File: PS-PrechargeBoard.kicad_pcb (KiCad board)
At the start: 2 copper layers, 230 parts, among them IC1 LM74502DDFR, IC2 TCAN3413DR, J1 HV_Main, J10 SWD, J2 HV_Motor, J3 DIAG, J4 CAN_IN, J5 CAN_OUT, J6 DEBUG_NANO, J7 PRECHARGE_CTRL, J8 USB_C_Receptacle_USB2.0_16P, J9 SWD_Header, K1 DE1a-12V, K2 DE1a-12V, Q1 NMOS, Q2 NMOS, Q3 PSMN012-100YS, Q4 PSMN012-100YS, SW1 Reset, SW2 SW_SPDT, U1 TLV9002QDRQ1, U4 TLV9002QDRQ1, U7 MCP1826S, U8 STM32G473CETx, Y1 Crystal

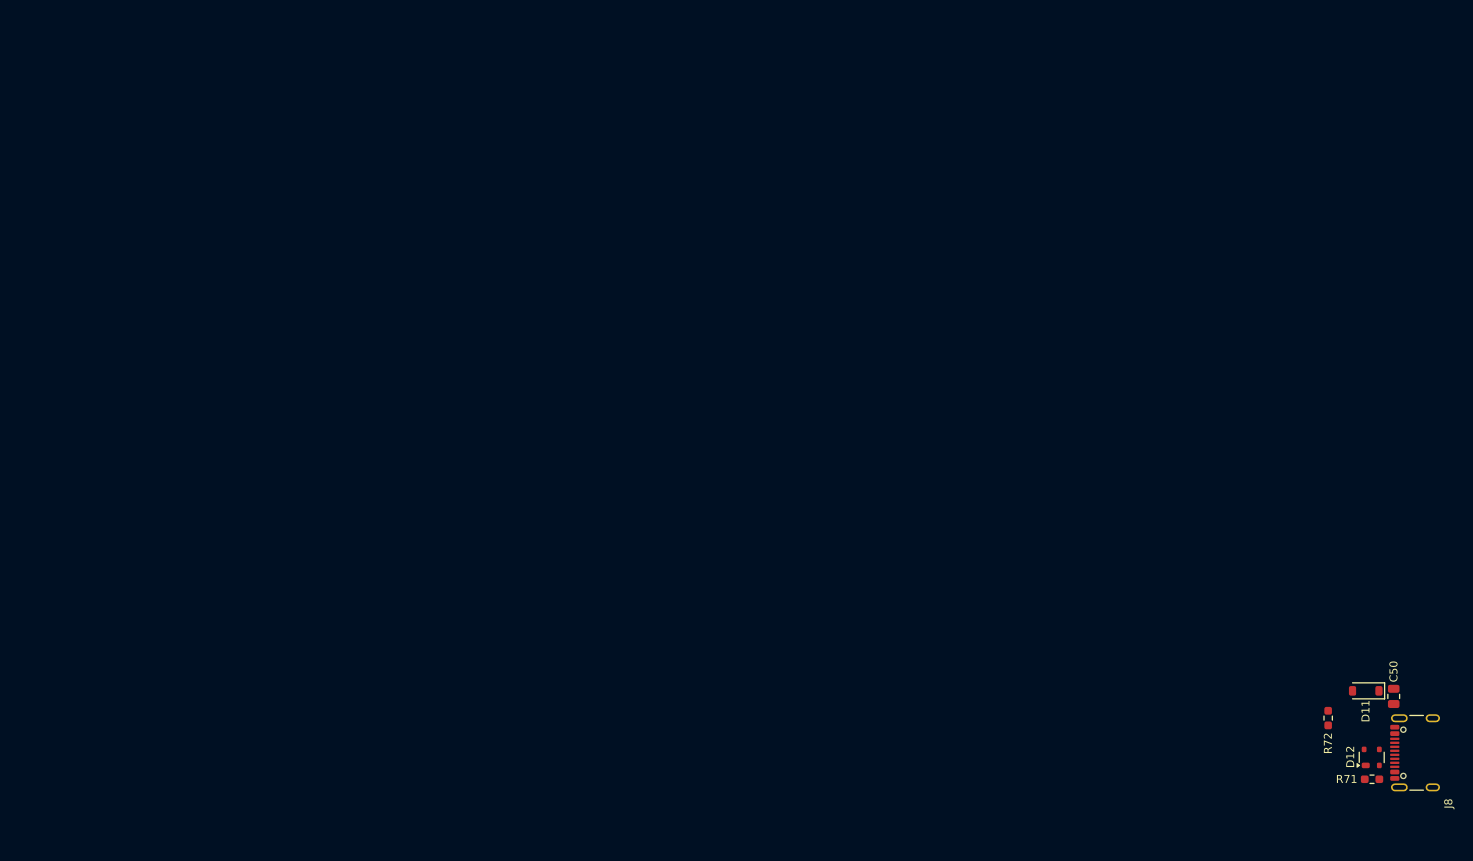
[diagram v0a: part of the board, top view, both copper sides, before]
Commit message: restored usb-c placement
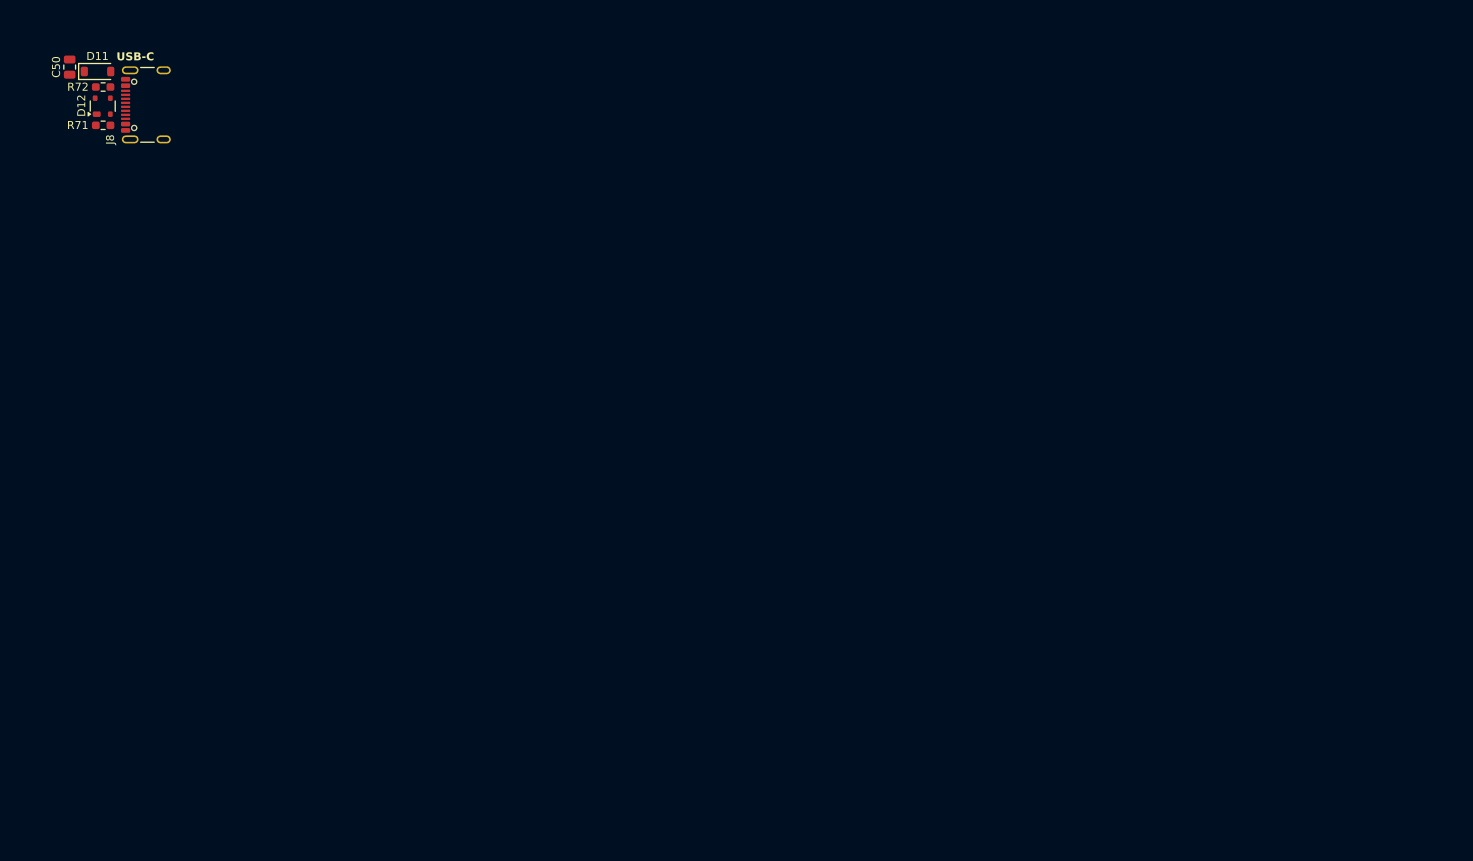
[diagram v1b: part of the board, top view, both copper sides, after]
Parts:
- moved C50 183.2 mm to (175.8, 80.2)
- moved R71 178.4 mm to (179.9, 87.5)
- moved D12 178.3 mm to (179.9, 85.1)
- moved J8 178.1 mm to (186.4, 84.9)
- moved D11 176.4 mm to (179.2, 80.8), turned to 0 degrees
- moved R72 172.3 mm to (179.9, 82.7), turned to 0 degrees
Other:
- board text added: "USB-C"
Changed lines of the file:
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@@
 	(footprint "Capacitor_SMD:C_0805_2012Metric"
 		(layer "F.Cu")
-		(at 341.273 158.886406 -90)
+		(at 175.768 80.222 -90)
 		(descr "Capacitor SMD 0805 (2012 Metric), square (rectangular) end terminal, IPC-7351 nominal, (Body size source: IPC-SM-782 page 76, https://www.pcb-3d.com/wordpress/wp-content/uploads/ipc-sm-782a_amendment_1_and_2.pdf, https://docs.google.com/spreadsheets/d/1BsfQQcO9C6DZCsRaXUlFlo91Tg2WpOkGARC1WS5S8t0/edit?usp=sharing)")
 		(tags "capacitor")
 		(property "Reference" "C50"
-			(at -3.109 0 90)
+			(at -0.0088 1.6764 90)
 			(layer "F.SilkS")
 			(effects
@@
 	(footprint "Resistor_SMD:R_0603_1608Metric_Pad0.98x0.95mm_HandSolder"
 		(layer "F.Cu")
-		(at 338.5615 169.241406)
+		(at 179.948 87.499667)
 		(descr "Resistor SMD 0603 (1608 Metric), square (rectangular) end terminal, IPC-7351 nominal with elongated pad for handsoldering. (Body size source: IPC-SM-782 page 72, https://www.pcb-3d.com/wordpress/wp-content/uploads/ipc-sm-782a_amendment_1_and_2.pdf)")
 		(tags "resistor handsolder")
@@
 	(footprint "Package_TO_SOT_SMD:SOT-143"
 		(layer "F.Cu")
-		(at 338.522 166.513406 90)
+		(at 179.898 85.106 90)
 		(descr "SOT-143 https://www.nxp.com/docs/en/package-information/SOT143B.pdf")
 		(tags "SOT-143")
@@
 	(footprint "Resistor_SMD:R_0603_1608Metric_Pad0.98x0.95mm_HandSolder"
 		(layer "F.Cu")
-		(at 333.077 161.597906 90)
+		(at 179.948 82.712334)
 		(descr "Resistor SMD 0603 (1608 Metric), square (rectangular) end terminal, IPC-7351 nominal with elongated pad for handsoldering. (Body size source: IPC-SM-782 page 72, https://www.pcb-3d.com/wordpress/wp-content/uploads/ipc-sm-782a_amendment_1_and_2.pdf)")
 		(tags "resistor handsolder")
 		(property "Reference" "R72"
-			(at -3.1515 0 90)
+			(at -3.1515 0 0)
 			(layer "F.SilkS")
 			(effects
@@
 		)
 		(property "Value" "5.1k"
-			(at 0 1.43 90)
+			(at 0 1.43 0)
 			(layer "F.Fab")
 			(effects
@@
 		)
 		(property "Datasheet" ""
-			(at 0 0 90)
+			(at 0 0 0)
 			(layer "F.Fab")
 			(hide yes)
@@
 		)
 		(property "Description" "Resistor"
-			(at 0 0 90)
+			(at 0 0 0)
 			(layer "F.Fab")
 			(hide yes)
@@
 		)
 		(property "LCSC P/N" "C23186"
-			(at 0 0 90)
+			(at 0 0 0)
 			(unlocked yes)
 			(layer "F.Fab")
@@
 		)
 		(property "P/N" "0603WAF5101T5E"
-			(at 0 0 90)
+			(at 0 0 0)
 			(unlocked yes)
 			(layer "F.Fab")
@@
 		)
 		(fp_text user "${REFERENCE}"
-			(at 0 0 90)
+			(at 0 0 0)
 			(layer "F.Fab")
 			(effects
@@
 		)
 		(pad "1" smd roundrect
-			(at -0.9125 0 90)
+			(at -0.9125 0)
 			(size 0.975 0.95)
 			(layers "F.Cu" "F.Mask" "F.Paste")
@@
 		)
 		(pad "2" smd roundrect
-			(at 0.9125 0 90)
+			(at 0.9125 0)
 			(size 0.975 0.95)
 			(layers "F.Cu" "F.Mask" "F.Paste")
@@
 	(footprint "LHRS_Connectors:USB_C_Receptacle_GCT_USB4105-xx-A_16P_TopMnt_Horizontal"
 		(layer "F.Cu")
-		(at 345.083 165.937406 90)
+		(at 186.436 84.942 90)
 		(descr "USB 2.0 Type C Receptacle, GCT, 16P, top mounted, horizontal, 5A: https://gct.co/files/drawings/usb4105.pdf")
 		(tags "USB C Type-C Receptacle SMD USB 2.0 16P 16C USB4105-15-A USB4105-15-A-060 USB4105-15-A-120 USB4105-GF-A USB4105-GF-A-060 USB4105-GF-A-120")
 		(property "Reference" "J8"
-			(at -6.35 3.048 90)
+			(at -4.339 -5.588 90)
 			(unlocked yes)
 			(layer "F.SilkS")
@@
 	(footprint "Diode_SMD:D_SOD-123"
 		(layer "F.Cu")
-		(at 337.776 158.192406 180)
+		(at 179.248 80.772)
 		(descr "SOD-123")
 		(tags "SOD-123")
 		(property "Reference" "D11"
-			(at -0.001 -2.54 90)
+			(at -0.001 -1.901667 180)
 			(layer "F.SilkS")
 			(effects
@@
 		)
 		(property "Datasheet" ""
-			(at 0 0 180)
+			(at 0 0 0)
 			(unlocked yes)
 			(layer "F.Fab")
@@
 		)
 		(property "Description" "Schottky diode"
-			(at 0 0 180)
+			(at 0 0 0)
 			(unlocked yes)
 			(layer "F.Fab")
@@
 		)
 		(property "P/N" "BAT760-7"
-			(at 0 0 180)
+			(at 0 0 0)
 			(unlocked yes)
 			(layer "F.Fab")
@@
 		)
 		(property "LCSC P/N" "C82544"
-			(at 0 0 180)
+			(at 0 0 0)
 			(unlocked yes)
 			(layer "F.Fab")
@@
 		(duplicate_pad_numbers_are_jumpers no)
 		(fp_line
-			(start -2.36 1)
-			(end 1.65 1)
+			(start -2.36 -1)
+			(end -2.36 1)
 			(stroke
 				(width 0.12)
@@
 		)
 		(fp_line
-			(start -2.36 -1)
-			(end -2.36 1)
+			(start -2.36 1)
+			(end 1.65 1)
 			(stroke
 				(width 0.12)
@@
 		)
 		(fp_line
-			(start 2.35 1.15)
+			(start -2.35 -1.15)
 			(end -2.35 1.15)
 			(stroke
@@
 		)
 		(fp_line
-			(start 2.35 -1.15)
-			(end 2.35 1.15)
+			(start -2.35 -1.15)
+			(end 2.35 -1.15)
 			(stroke
 				(width 0.05)
@@
 		)
 		(fp_line
-			(start -2.35 -1.15)
-			(end 2.35 -1.15)
+			(start 2.35 -1.15)
+			(end 2.35 1.15)
 			(stroke
 				(width 0.05)
@@
 		)
 		(fp_line
-			(start -2.35 -1.15)
+			(start 2.35 1.15)
 			(end -2.35 1.15)
 			(stroke
@@
 		)
 		(fp_line
-			(start 1.4 0.9)
-			(end -1.4 0.9)
+			(start -1.4 -0.9)
+			(end 1.4 -0.9)
 			(stroke
 				(width 0.1)
@@
 		)
 		(fp_line
-			(start 1.4 -0.9)
-			(end 1.4 0.9)
+			(start -1.4 0.9)
+			(end -1.4 -0.9)
 			(stroke
 				(width 0.1)
@@
 		)
 		(fp_line
-			(start 0.25 0.4)
+			(start -0.75 0)
 			(end -0.35 0)
 			(stroke
@@
 		)
 		(fp_line
-			(start 0.25 0)
-			(end 0.75 0)
+			(start -0.35 0)
+			(end -0.35 -0.55)
 			(stroke
 				(width 0.1)
@@
 		)
 		(fp_line
-			(start 0.25 -0.4)
-			(end 0.25 0.4)
+			(start -0.35 0)
+			(end -0.35 0.55)
 			(stroke
 				(width 0.1)
@@
 		)
 		(fp_line
-			(start -0.35 0)
-			(end -0.35 0.55)
+			(start 0.25 -0.4)
+			(end 0.25 0.4)
 			(stroke
 				(width 0.1)
@@
 		)
 		(fp_line
-			(start -0.35 0)
-			(end -0.35 -0.55)
+			(start 0.25 0)
+			(end 0.75 0)
 			(stroke
 				(width 0.1)
@@
 		)
 		(fp_line
-			(start -0.75 0)
+			(start 0.25 0.4)
 			(end -0.35 0)
 			(stroke
@@
 		)
 		(fp_line
-			(start -1.4 0.9)
-			(end -1.4 -0.9)
+			(start 1.4 -0.9)
+			(end 1.4 0.9)
 			(stroke
 				(width 0.1)
@@
 		)
 		(fp_line
-			(start -1.4 -0.9)
-			(end 1.4 -0.9)
+			(start 1.4 0.9)
+			(end -1.4 0.9)
 			(stroke
 				(width 0.1)
@@
 		)
 		(pad "1" smd roundrect
-			(at -1.65 0 180)
+			(at -1.65 0)
 			(size 0.9 1.2)
 			(layers "F.Cu" "F.Mask" "F.Paste")
@@
 		)
 		(pad "2" smd roundrect
-			(at 1.65 0 180)
+			(at 1.65 0)
 			(size 0.9 1.2)
 			(layers "F.Cu" "F.Mask" "F.Paste")
@@
 		)
 	)
+	(gr_text "USB-C"
+		(at 181.61 79.502 0)
+		(layer "F.SilkS")
+		(effects
+			(font
+				(size 1 1)
+				(thickness 0.2)
+				(bold yes)
+			)
+			(justify left bottom)
+		)
+	)
 	(gr_text "Main Precharge "
 		(at 85.75681 66.722766 90)
@@
 		)
 	)
+	(group ""
+		(members "30c317c0-166f-4138-87f3-9f8309e86ead" "745d89ca-e13b-4196-b063-be9ce27b8f92"
+			"98889215-c0ed-45cf-a5c2-d460b8110712" "b0dbe07d-f4ad-4f53-bb42-7bba249caea2"
+			"b126f00e-3486-45a0-9c2a-e122d2dbbd07" "b9c265ff-ae24-4e46-81cd-534d7b0bfe95"
+			"fe1b8a1b-92c0-46a2-bd88-c4bfb9b639ae"
+		)
+	)

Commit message: can-transceiver & ldo placement
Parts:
- moved TP14 234.7 mm to (65.0, -67.9)
- moved C53 209.6 mm to (174.9, 106.0), turned to 180 degrees
- moved TP_3.3V1 209.3 mm to (159.8, 102.2)
- moved C52 204.5 mm to (163.0, 105.9), turned to 180 degrees
- moved U7 202.4 mm to (156.7, 107.9), turned to 180 degrees
- moved C51 200.6 mm to (163.0, 109.9), turned to 180 degrees
- moved D14 200.3 mm to (186.3, 109.9)
- moved J3 199.0 mm to (67.2, -61.7)
- moved IC2 198.9 mm to (180.6, 107.8)
- moved D13 198.5 mm to (163.2, 107.9)
- moved C55 197.6 mm to (175.2, 109.3), turned to 180 degrees
- moved C54 197.0 mm to (175.2, 107.8), turned to 180 degrees
- moved JP1 196.8 mm to (181.9, 112.5), turned to -90 degrees
- moved R73 192.9 mm to (186.1, 107.3)
- moved C56 192.3 mm to (186.1, 105.8)
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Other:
- board text added: "CAN-Transceiver"
- board text added: "LDO"
- board text removed: "MCU"

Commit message: mcu placement
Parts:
- moved TP13 221.5 mm to (182.4, 117.1), turned to 90 degrees
- moved TP14 221.3 mm to (186.4, 117.1), turned to 90 degrees
- moved J3 201.9 mm to (177.3, 107.6), turned to 90 degrees
- moved R75 188.0 mm to (171.1, 116.9)
- moved R77 184.5 mm to (171.1, 118.4)
- moved R78 183.5 mm to (171.1, 119.9)
- moved R79 182.6 mm to (156.3, 106.0)
- moved R80 182.6 mm to (156.3, 104.5)
- moved TP11 181.2 mm to (178.1, 117.1), turned to 90 degrees
- moved J9 178.5 mm to (155.7, 99.6), turned to -90 degrees
- moved FB1 178.0 mm to (172.7, 111.5), turned to -90 degrees
- moved C58 173.9 mm to (164.6, 116.6), turned to 180 degrees
- moved C57 173.4 mm to (161.3, 116.6), turned to 180 degrees
- moved C60 171.2 mm to (164.2, 99.3)
- moved C62 171.2 mm to (162.4, 99.4)
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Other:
- board text added: "MCU"
